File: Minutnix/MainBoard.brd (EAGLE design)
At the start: 235 x 80 mm, 132 parts, among them IC1 MEGA8-AI, IC6 TP4056, IC7 FT232RL, IC9 SC4503, Q4 32.768kHz, T1 DMN3024LSD, X1 FH12-12S-0.5SH, X2 87438-03, X3 87438-03

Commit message: 7segm lib + board
Corrections on consistency and erc errors
readded 7 segm. custom lib
Partial components placement and routing tries
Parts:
- removed C11: 10u, capacitor-wima:C2.5-2
- removed C12, C13: 0.1u, capacitor-wima:C2.5-2
- removed C24: 10pF, capacitor-wima:C2.5-2
- removed C25: 10 - 22uF, capacitor-wima:C2.5-2
- removed C26: 56nF, capacitor-wima:C2.5-2
- removed C27: 4.7u, capacitor-wima:C2.5-2
- removed IC1: MEGA8-AI, atmel:TQFP32-08
- removed IC6: TP4056, TP4056:SOP-8
- removed IC9: SC4503, v-reg-3:SOT23-5
- removed L3: 4.237H, inductor-neosid:MS42
- removed LED3, LED4: (no value), led:CHIPLED_0603
- removed R37, R38: 1k, rcl:R1206
- removed R41: 1.2k, rcl:R1206
- removed R53: 15k, rcl:R1206
- removed R54: 620k, rcl:R1206
- removed R55: 100k, rcl:R1206
- removed S1: (no value), switch:MS243
- removed SHOTTKYDIODE2: S2A, s2x_10:DO214AA
- removed T1: DMN3024LSD, FS8205A:TSSOP-8
- removed U$2: DW01A, DW01A:SOT23-6
- removed X3: 87438-03, con-molex:87438-03
- added C5: 100n, rcl:C0603
- added C5SPRAWDZGOOOOOOOOOOOOOOOOOOOOOOOOOOOOOOOOOOOOOOOOOOO, C5SPRAWDZGOOOOOOOOOOOOOOOOOOOOOOOOOOOOOOOOOOOOOOOOOOO1: 10u, rcl:C3216
- added CHRG_LED, STDBY_LED: (no value), led:CHIPLED_0603
- added IC2: (no value), v-reg-2:SOT223
- added IC3: TP4056, TP4056:SOP-8
- added J_REG_9V_1: 9V_VOLTAGE_REGULATOR, Pololu_vreg:9V_VOLTAGE_REGULATOR
- added R32, R35: 51R, rcl:R0603
- added R48: 1.2k, rcl:R0603
- added U$1: SW, MySwitch:SWBOTLAND
- added X4: JST-XH-03-PIN-LONG-PAD, Rembrandt Electronics - JST XH Connectors v1-0:JST-XH-03-PACKAGE-LONG-PAD
- R34, R50: value 400R -> 220R
- R39: value 1k -> 620R-1k; device rcl:R1206 -> rcl:R0603
- R40: value 100 -> 620R-1k; device rcl:R1206 -> rcl:R0603
- R47, R52, R64, R65, R66: value 2k2 -> 620R-1k
- X2: value 87438-03 -> JST-XH-03-PIN-LONG-PAD; device con-molex:87438-03 -> Rembrandt Electronics - JST XH Connectors v1-0:JST-XH-03-PACKAGE-LONG-PAD
- moved JP13 344.6 mm to (197.0, 29.1)
- moved R19 342.2 mm to (196.9, 10.2), flipped to the bottom, turned to 90 degrees
- moved LS_SEC_REG 336.5 mm to (195.3, 22.3), flipped to the bottom
- moved JP20 336.4 mm to (161.5, 50.6)
- moved R18 335.6 mm to (194.3, 10.2), flipped to the bottom, turned to 90 degrees
- moved R17 329.0 mm to (191.6, 10.2), flipped to the bottom, turned to 270 degrees
- moved R21 327.2 mm to (196.9, 65.4), flipped to the bottom, turned to 270 degrees
- moved R20 324.7 mm to (199.3, 65.4), flipped to the bottom, turned to 270 degrees
- moved R47 312.4 mm to (132.5, 58.9), flipped to the bottom, turned to 270 degrees
- moved JP19 308.0 mm to (132.0, 41.8), turned to 90 degrees
- moved MS_SEC_REG 303.0 mm to (142.5, 22.3), flipped to the bottom
- moved JP16 301.8 mm to (141.5, 44.1)
- moved JP18 301.2 mm to (132.0, 47.0), turned to 90 degrees
- moved R16 298.8 mm to (191.6, 65.4), flipped to the bottom, turned to 270 degrees
- moved R40 298.3 mm to (186.8, 41.9), turned to 180 degrees
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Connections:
- removed net +3V3: C1.2, IC7.17, RXLED.A, TXLED.A
- removed net BATTERY-: C13.1, T1.6, T1.7, U$2.6, X3.3
- removed net DI: JP16.1
- removed net N$100: LED3.C, R37.2
- removed net N$101: LED4.C, R38.2
- removed net N$102: T1.4, U$2.3
- removed net N$104: T1.1, T1.8
- removed net N$105: T1.5, U$2.1
- removed net N$106: R39.2, U$2.2
- removed net N$109: C13.2, R40.2, U$2.5
- removed net N$111: IC6.2, R41.2
- removed net N$113: IC9.1, L3.1, SHOTTKYDIODE2.A
- removed net N$118: C26.2, IC9.4, R53.2
- removed net N$119: C24.1, IC9.3, R54.2, R55.1
- removed net N$98: IC6.7, R37.1
- removed net N$99: IC6.6, R38.1
- removed net VDD1: LSDIGIT_MINUTES.COM1, LSDIGIT_MINUTES.COM8, LSDIGIT_SECONDS.COM1, LSDIGIT_SECONDS.COM8, MSDIGIT_MINUTES.COM1, MSDIGIT_MINUTES.COM8, MSDIGIT_SECONDS.COM1, MSDIGIT_SECONDS.COM8
- new net N$1: R32.2, R50.1
- new net N$27: C1.2, IC7.17
- new net N$29: J_REG_9V_1.VIN, U$1.2
- new net N$49: R34.1, R35.2
- new net N$52: IC3.7, R39.2
- new net N$53: IC3.6, R40.2
- new net N$54: CHRG_LED.C, R39.1
- new net N$55: R40.1, STDBY_LED.C
- new net N$82: IC3.2, R48.1
- net +5V: now also C5.1, CHRG_LED.A, IC3.4, IC3.8, RXLED.A, STDBY_LED.A, TXLED.A, X4.1; no longer C12.2, IC6.4, IC6.8, LED3.A, LED4.A, X2.1
- net AREF: no longer IC1.20
- net AVCC: now also R57.1; no longer IC1.18
- net BATTERY+: now also IC3.5, U$1.1, X2.1; no longer C11.2, IC6.5, R40.1, S1.1, X3.1
- net BATTERY_S: now also X2.2; no longer X3.2
- net BUZZ: no longer IC1.13
- net D_BLOCK: no longer IC1.14
- net D_RCK: no longer IC1.12
- net D_SCK: no longer IC1.17
- net D_SI: no longer IC1.15
- net EXP_INT: no longer IC1.32
- net EXP_SCL: no longer IC1.28
- net EXP_SDA: no longer IC1.27
- net GND: now also C5.2, C5SPRAWDZGOOOOOOOOOOOOOOOOOOOOOOOOOOOOOOOOOOOOOOOOOOO.2, C5SPRAWDZGOOOOOOOOOOOOOOOOOOOOOOOOOOOOOOOOOOOOOOOOOOO1.1, C5SPRAWDZGOOOOOOOOOOOOOOOOOOOOOOOOOOOOOOOOOOOOOOOOOOO1.2, IC2.1, IC3.1, IC3.3, J_REG_9V_1.GND, R48.2, U$1.3, X2.3, X4.2; no longer C11.1, C12.1, C25.1, C26.1, C27.1, IC1.3, IC1.5, IC6.1, IC6.3, IC9.2, R39.1, R41.1, R55.2, T1.2, T1.3, X2.2
- net GNDA: no longer IC1.21
- net LIGHT_SENS: no longer IC1.23
- net L_COUNTER: no longer IC1.24
- net L_VOLUME: no longer IC1.26
- net L_WARNING: no longer IC1.25
- net MISO: no longer IC1.16
- net N$50: now also R32.1; no longer R50.1
- net N$51: now also R35.1; no longer R34.1
- net RESET: no longer IC1.29
- net RI: now also JP16.1
- net RXD: no longer IC1.30
- net S_VCC: no longer IC1.11, IC1.4, IC1.6
- net TXD: no longer IC1.31
- net UA1: no longer IC1.1
- net UA2: no longer IC1.2
- net UA3: no longer IC1.9
- net UA4: no longer IC1.19
- net UA5: no longer IC1.22
- net VCC: now also C5SPRAWDZGOOOOOOOOOOOOOOOOOOOOOOOOOOOOOOOOOOOOOOOOOOO.1, IC2.2, X4.3; no longer C27.2, IC1.10, IC9.5, L3.2, R53.1, S1.2, X2.3
- net VDD: now also IC2.3, J_REG_9V_1.VOUT, LSDIGIT_MINUTES.COM1, LSDIGIT_MINUTES.COM8, LSDIGIT_SECONDS.COM1, LSDIGIT_SECONDS.COM8, MSDIGIT_MINUTES.COM1, MSDIGIT_MINUTES.COM8, MSDIGIT_SECONDS.COM1, MSDIGIT_SECONDS.COM8; no longer C24.2, C25.2, R54.1, R57.1, SHOTTKYDIODE2.C
- net XTAL1: no longer IC1.7
- net XTAL2: no longer IC1.8
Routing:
- net VDD: track 0.00 -> 505.9 mm
- net GND: track 0.00 -> 50.6 mm
- net +5V: track 0.00 -> 36.3 mm
- net STOP/RESET: track 0.00 -> 19.1 mm
- net PLAY/PAUSE: track 0.00 -> 17.8 mm
- net COUNTER: track 0.00 -> 16.4 mm
- net WARNING: track 0.00 -> 15.0 mm
- net USBDM: track 0.00 -> 13.3 mm
- net USBDP: track 0.00 -> 11.9 mm
- net ENC_B: track 0.00 -> 11.2 mm
- net LIGHT_SENS: track 0.00 -> 10.4 mm
- net ENC_A: track 0.00 -> 9.54 mm
- net RTS: track 0.00 -> 8.15 mm
- net VOLUME: track 0.00 -> 6.67 mm
- net VCC: track 0.00 -> 6.28 mm
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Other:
- board size 235 x 80 mm -> 221.1 x 72.7 mm

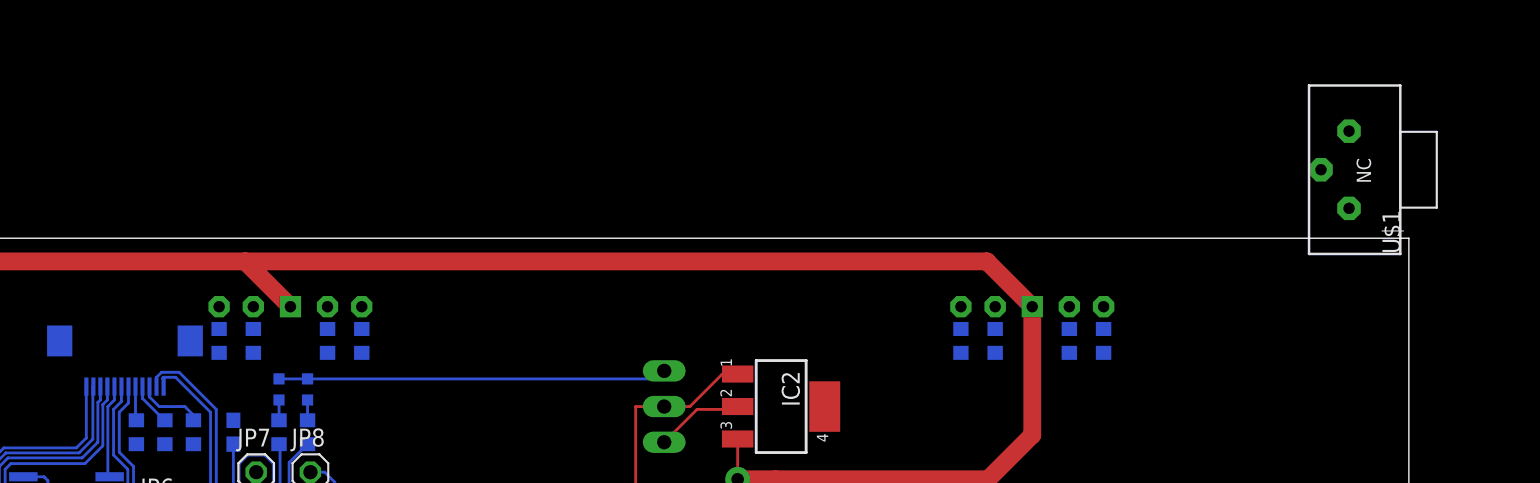
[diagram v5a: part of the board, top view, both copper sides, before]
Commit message: libs actualisation + drc rules for expander
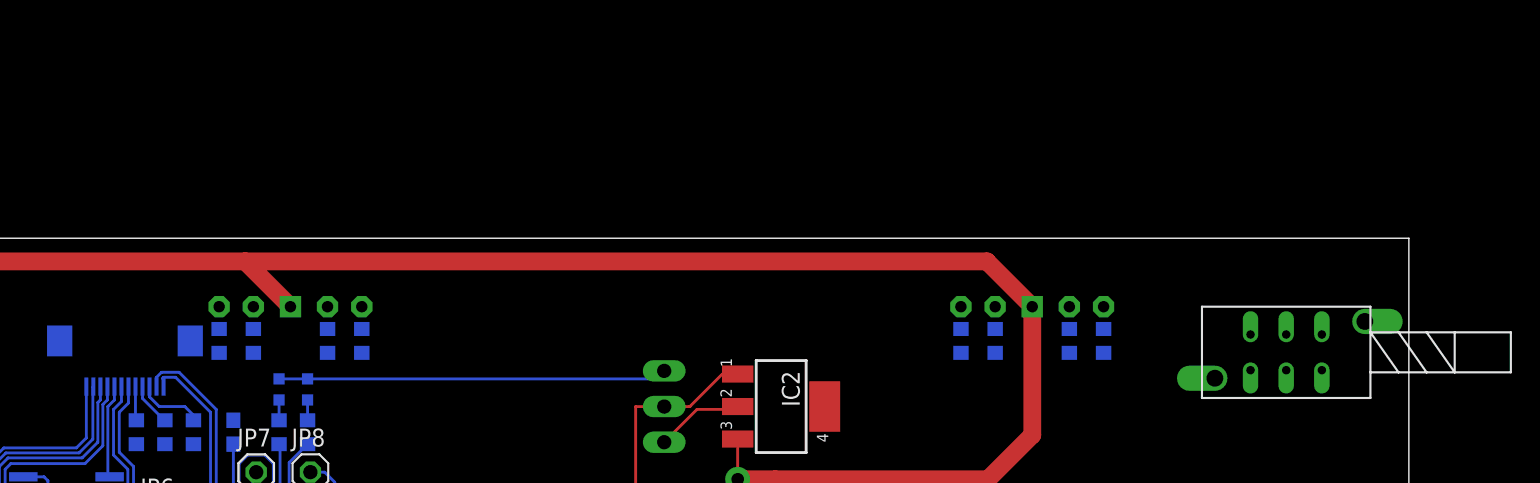
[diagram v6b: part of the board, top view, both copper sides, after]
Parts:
- removed U$1: SW, MySwitch:SWBOTLAND
- added U$2: X2, Isostat:MINI
- X1: value FH12-12S-0.5SH -> FH12-12S-0.5S_THINNER; device con-hirose:FH12-12S-0.5SH -> My_con-hirose:FH12-12S-0.5SH_THINER
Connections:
- removed net N$29: J_REG_9V_1.VIN, U$1.2
- new net N$81: J_REG_9V_1.VIN, U$2.2, U$2.5
- net BATTERY+: now also U$2.1, U$2.4; no longer U$1.1
- net GND: now also U$2.3, U$2.6; no longer U$1.3

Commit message: Consolidation of schematic + lib restore
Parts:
- SHOTTKYDIODE3: device s2x_10:DO214AA -> Shottky:DO214AA
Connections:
- net AVCC: now also L1.2, R57.2; no longer L1.1, R57.1
- net LIGHT_SENS: now also R57.3; no longer R57.2
- net S_VCC: now also L1.1; no longer L1.2
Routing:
- net VDD: track 505.9 -> 445.1 mm
- net LIGHT_SENS: track 10.4 -> 0.00 mm
- net GND: track 50.6 -> 49.4 mm

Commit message: lib update + board ongoing
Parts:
- removed SJ1: (no value), jumper:SJ
- moved C18 189.3 mm to (201.4, 18.1), flipped to the bottom, turned to 270 degrees
- moved R29 164.4 mm to (21.1, 17.5), flipped to the bottom, turned to 90 degrees
- moved C2 159.3 mm to (203.6, 59.1), flipped to the bottom
- moved C5SPRAWDZGOOOOOOOOOOOOOOOOOOOOOOOOOOOOOOOOOOOOOOOOOOO1 153.0 mm to (209.1, 67.7), flipped to the bottom
- moved C17 145.3 mm to (151.0, 17.9), flipped to the bottom, turned to 270 degrees
- moved C5SPRAWDZGOOOOOOOOOOOOOOOOOOOOOOOOOOOOOOOOOOOOOOOOOOO 140.9 mm to (177.6, 35.3), flipped to the bottom, turned to 180 degrees
- moved R30 134.2 mm to (67.1, 22.4), flipped to the bottom, turned to 180 degrees
- moved C30 130.5 mm to (156.9, 34.3), flipped to the bottom
- moved C3 127.4 mm to (172.5, 62.2), flipped to the bottom, turned to 90 degrees
- moved C4 122.5 mm to (134.1, 35.6), flipped to the bottom
- moved C29 122.0 mm to (156.9, 40.0), flipped to the bottom
- moved R50 115.0 mm to (109.9, 31.1), flipped to the bottom, turned to 270 degrees
- moved C5 111.7 mm to (174.5, 62.2), flipped to the bottom, turned to 90 degrees
- moved C16 109.0 mm to (88.6, 17.9), flipped to the bottom, turned to 270 degrees
- moved C15 107.8 mm to (34.3, 17.7), flipped to the bottom, turned to 270 degrees
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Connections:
- removed net N$30: R61.2, SJ1.2
- removed net N$50: COLON1.K, R32.1
- removed net N$51: COLON2.K, R35.1
- new net N$29: COLON2.A, R34.2
- new net N$56: COLON1.A, R50.2
- net BATTERY+: now also C5SPRAWDZGOOOOOOOOOOOOOOOOOOOOOOOOOOOOOOOOOOOOOOOOOOO1.2
- net GND: now also Q4.SHEILD, U$2.CASE1, U$2.CASE2; no longer C5SPRAWDZGOOOOOOOOOOOOOOOOOOOOOOOOOOOOOOOOOOOOOOOOOOO1.2, PHOTORES.1
- net GNDA: now also PHOTORES.1
- net N$2: now also COLON1.K; no longer R50.2
- net N$20: now also COLON2.K; no longer R34.2
- net UP1: now also R61.2; no longer SJ1.1
- net VCC: now also IC2.4, R32.1, R35.1; no longer COLON1.A, COLON2.A
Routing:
- net VCC: track 6.28 -> 306.2 mm, vias 0 -> 7
- net GND: track 49.4 -> 305.7 mm, vias 0 -> 1
- net D_BLOCK: track 0.00 -> 194.2 mm, vias 0 -> 4
- net D_SCK: track 0.00 -> 190.8 mm, vias 0 -> 5
- net D_RCK: track 0.00 -> 190.4 mm, vias 0 -> 4
- net N$24: track 0.00 -> 184.4 mm, vias 0 -> 4
- net +5V: track 36.3 -> 147.3 mm
- net BATTERY+: track 0.00 -> 92.7 mm
- net VDD: track 445.1 -> 523.3 mm
- net N$81: track 0.00 -> 75.8 mm
- net D_SI: track 0.00 -> 64.4 mm, vias 0 -> 2
- net N$78: track 0.00 -> 58.0 mm, vias 0 -> 2
- net N$43: track 4.39 -> 59.7 mm, vias 0 -> 2
- net LIGHT_SENS: track 0.00 -> 53.4 mm
- net N$58: track 0.00 -> 53.0 mm, vias 0 -> 1
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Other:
- board size 221.1 x 72.7 mm -> 222.3 x 73.3 mm
